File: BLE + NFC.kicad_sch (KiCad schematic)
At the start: 16 parts, among them IC5 nRF52832-CIAA-G-R7, Y2 Crystal_GND24

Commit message: progressed layout
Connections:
- net NRF_RXD: now also IC5.H3 (P0.16_/TRACEDATA[1]); no longer IC5.F4 (P0.11)
- net NRF_SDA: now also IC5.E7 (P0.05/_AIN3); no longer IC5.F6 (P0.07)
- net NRF_TXD: now also IC5.H4 (P0.15/TRACEDATA[2]); no longer IC5.H6 (P0.12)
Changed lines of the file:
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@@
     (stroke (width 0) (type default))
   )
-  (wire (pts (xy 176.53 107.95) (xy 179.07 107.95))
+  (wire (pts (xy 176.53 100.33) (xy 179.07 100.33))
     (stroke (width 0) (type default))
   )
@@
     (stroke (width 0) (type default))
   )
-  (wire (pts (xy 176.53 115.57) (xy 179.07 115.57))
+  (wire (pts (xy 176.53 120.65) (xy 179.07 120.65))
     (stroke (width 0) (type default))
   )
@@
     (stroke (width 0) (type default))
   )
-  (wire (pts (xy 176.53 110.49) (xy 179.07 110.49))
+  (wire (pts (xy 176.53 97.79) (xy 179.07 97.79))
     (stroke (width 0) (type default))
   )
@@
     )
   )
-  (hierarchical_label "NRF_TXD" (shape input) (at 179.07 107.95 0) (fields_autoplaced)
-    (effects (font (size 1.27 1.27)) (justify left))
-    (property "Intersheetrefs" "${INTERSHEET_REFS}" (at 189.3965 107.95 0)
-      (effects (font (size 1.27 1.27)) (justify left) hide)
-    )
-  )
-  (hierarchical_label "NRF_RXD" (shape input) (at 179.07 110.49 0) (fields_autoplaced)
-    (effects (font (size 1.27 1.27)) (justify left))
-    (property "Intersheetrefs" "${INTERSHEET_REFS}" (at 189.6989 110.49 0)
-      (effects (font (size 1.27 1.27)) (justify left) hide)
-    )
-  )
-  (hierarchical_label "NRF_SDA" (shape input) (at 179.07 115.57 0) (fields_autoplaced)
-    (effects (font (size 1.27 1.27)) (justify left))
-    (property "Intersheetrefs" "${INTERSHEET_REFS}" (at 190.2006 115.57 0)
+  (hierarchical_label "NRF_TXD" (shape input) (at 179.07 100.33 0) (fields_autoplaced)
+    (effects (font (size 1.27 1.27)) (justify left))
+    (property "Intersheetrefs" "${INTERSHEET_REFS}" (at 189.3965 97.79 0)
+      (effects (font (size 1.27 1.27)) (justify left) hide)
+    )
+  )
+  (hierarchical_label "NRF_RXD" (shape input) (at 179.07 97.79 0) (fields_autoplaced)
+    (effects (font (size 1.27 1.27)) (justify left))
+    (property "Intersheetrefs" "${INTERSHEET_REFS}" (at 189.6989 100.33 0)
+      (effects (font (size 1.27 1.27)) (justify left) hide)
+    )
+  )
+  (hierarchical_label "NRF_SDA" (shape input) (at 179.07 120.65 0) (fields_autoplaced)
+    (effects (font (size 1.27 1.27)) (justify left))
+    (property "Intersheetrefs" "${INTERSHEET_REFS}" (at 190.2006 120.65 0)
       (effects (font (size 1.27 1.27)) (justify left) hide)
     )
@@
   )
   (symbol (lib_id "ARMband:nRF52832-CIAA-G-R7") (at 120.65 71.12 0) (unit 1)
-    (in_bom yes) (on_board yes) (dnp no) (fields_autoplaced)
+    (in_bom yes) (on_board yes) (dnp no)
     (property "Reference" "IC5" (at 155.6259 140.97 0)
       (effects (font (size 1.27 1.27)) (justify left))

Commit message: added missing MFN numbers
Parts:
- AE1, C25, C8, IC5, L5, L6, Y2: sourced (none) -> y
- C25: MFN (none) -> 581-04025A101KAT2A62; sourced (none) -> y
- C8: MFN 187-CL05A475KQ5NRNC -> 187-CL05A475KQ5NRNC; sourced (none) -> y
- JP1: sourced (none) -> dc
- L4: MFN 810-MLZ1608E100MT -> 810-MLZ1608E100MT; sourced (none) -> y
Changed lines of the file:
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@@
+      (effects (font (size 1.27 1.27)) hide)
+    )
+    (property "sourced" "y" (at 120.65 71.12 0)
       (effects (font (size 1.27 1.27)) hide)
     )
@@
       (effects (font (size 1.27 1.27)) hide)
     )
-    (property "MFN" " 810-MLZ1608E100MT " (at 115.57 111.76 90)
+    (property "MFN" "810-MLZ1608E100MT " (at 115.57 111.76 90)
+      (effects (font (size 1.27 1.27)) hide)
+    )
+    (property "sourced" "y" (at 115.57 111.76 0)
       (effects (font (size 1.27 1.27)) hide)
     )
@@
       (effects (font (size 1.27 1.27)) hide)
     )
+    (property "sourced" "y" (at 52.07 50.8 0)
+      (effects (font (size 1.27 1.27)) hide)
+    )
     (pin "1")
     (pin "2")
@@
     )
     (property "MFN" "581-CX2016SA24DHLLG3 " (at 83.82 86.36 0)
+      (effects (font (size 1.27 1.27)) hide)
+    )
+    (property "sourced" "y" (at 83.82 86.36 0)
       (effects (font (size 1.27 1.27)) hide)
     )
@@
     )
     (property "MFN" "80-C0402C104M4V " (at 140.97 43.18 0)
+      (effects (font (size 1.27 1.27)) hide)
+    )
+    (property "sourced" "y" (at 140.97 43.18 0)
       (effects (font (size 1.27 1.27)) hide)
     )
@@
       (effects (font (size 1.27 1.27)) hide)
     )
+    (property "sourced" "y" (at 107.95 111.76 0)
+      (effects (font (size 1.27 1.27)) hide)
+    )
     (pin "1")
     (pin "2")
@@
     )
     (property "MFN" "603-AC0201JNPO9BN120 " (at 92.71 91.44 0)
+      (effects (font (size 1.27 1.27)) hide)
+    )
+    (property "sourced" "y" (at 92.71 91.44 0)
       (effects (font (size 1.27 1.27)) hide)
     )
@@
       (effects (font (size 1.27 1.27)) hide)
     )
-    (property "MFN" "" (at 38.1 25.4 0)
+    (property "MFN" "581-04025A101KAT2A62 " (at 38.1 25.4 0)
+      (effects (font (size 1.27 1.27)) hide)
+    )
+    (property "sourced" "y" (at 38.1 25.4 0)
       (effects (font (size 1.27 1.27)) hide)
     )
@@
       (effects (font (size 1.27 1.27)) hide)
     )
-    (property "MFN" " 187-CL05A475KQ5NRNC " (at 128.27 43.18 0)
+    (property "MFN" "187-CL05A475KQ5NRNC " (at 128.27 43.18 0)
+      (effects (font (size 1.27 1.27)) hide)
+    )
+    (property "sourced" "y" (at 128.27 43.18 0)
       (effects (font (size 1.27 1.27)) hide)
     )
@@
       (effects (font (size 1.27 1.27)) hide)
     )
+    (property "sourced" "y" (at 39.37 55.88 0)
+      (effects (font (size 1.27 1.27)) hide)
+    )
     (pin "1")
     (pin "2")
@@
       (effects (font (size 1.27 1.27)) hide)
     )
+    (property "sourced" "dc" (at 133.35 36.83 0)
+      (effects (font (size 1.27 1.27)) hide)
+    )
     (pin "1")
     (pin "2")
@@
       (effects (font (size 1.27 1.27)) hide)
     )
+    (property "sourced" "y" (at 74.93 91.44 0)
+      (effects (font (size 1.27 1.27)) hide)
+    )
     (pin "1")
     (pin "2")
@@
     )
     (property "MFN" "791-0402N0R8B160CT " (at 33.02 60.96 0)
+      (effects (font (size 1.27 1.27)) hide)
+    )
+    (property "sourced" "y" (at 33.02 60.96 0)
       (effects (font (size 1.27 1.27)) hide)
     )
@@
       (effects (font (size 1.27 1.27)) hide)
     )
+    (property "sourced" "y" (at 162.56 43.18 0)
+      (effects (font (size 1.27 1.27)) hide)
+    )
     (pin "1")
     (pin "2")
@@
       (effects (font (size 1.27 1.27)) hide)
     )
+    (property "sourced" "y" (at 90.17 115.57 0)
+      (effects (font (size 1.27 1.27)) hide)
+    )
     (pin "1")
     (pin "2")
@@
       (effects (font (size 1.27 1.27)) hide)
     )
-    (property "MFN" "" (at 38.1 30.48 0)
-      (effects (font (size 1.27 1.27)) hide)
-    )
+    (property "MFN" "581-04025A101KAT2A62 " (at 38.1 30.48 0)
+      (effects (font (size 1.27 1.27)) hide)
+    )
+    (property "sourced" "y" (at 38.1 30.48 0)
+      (effects (font (size 1.27 1.27)) hide)
+    )

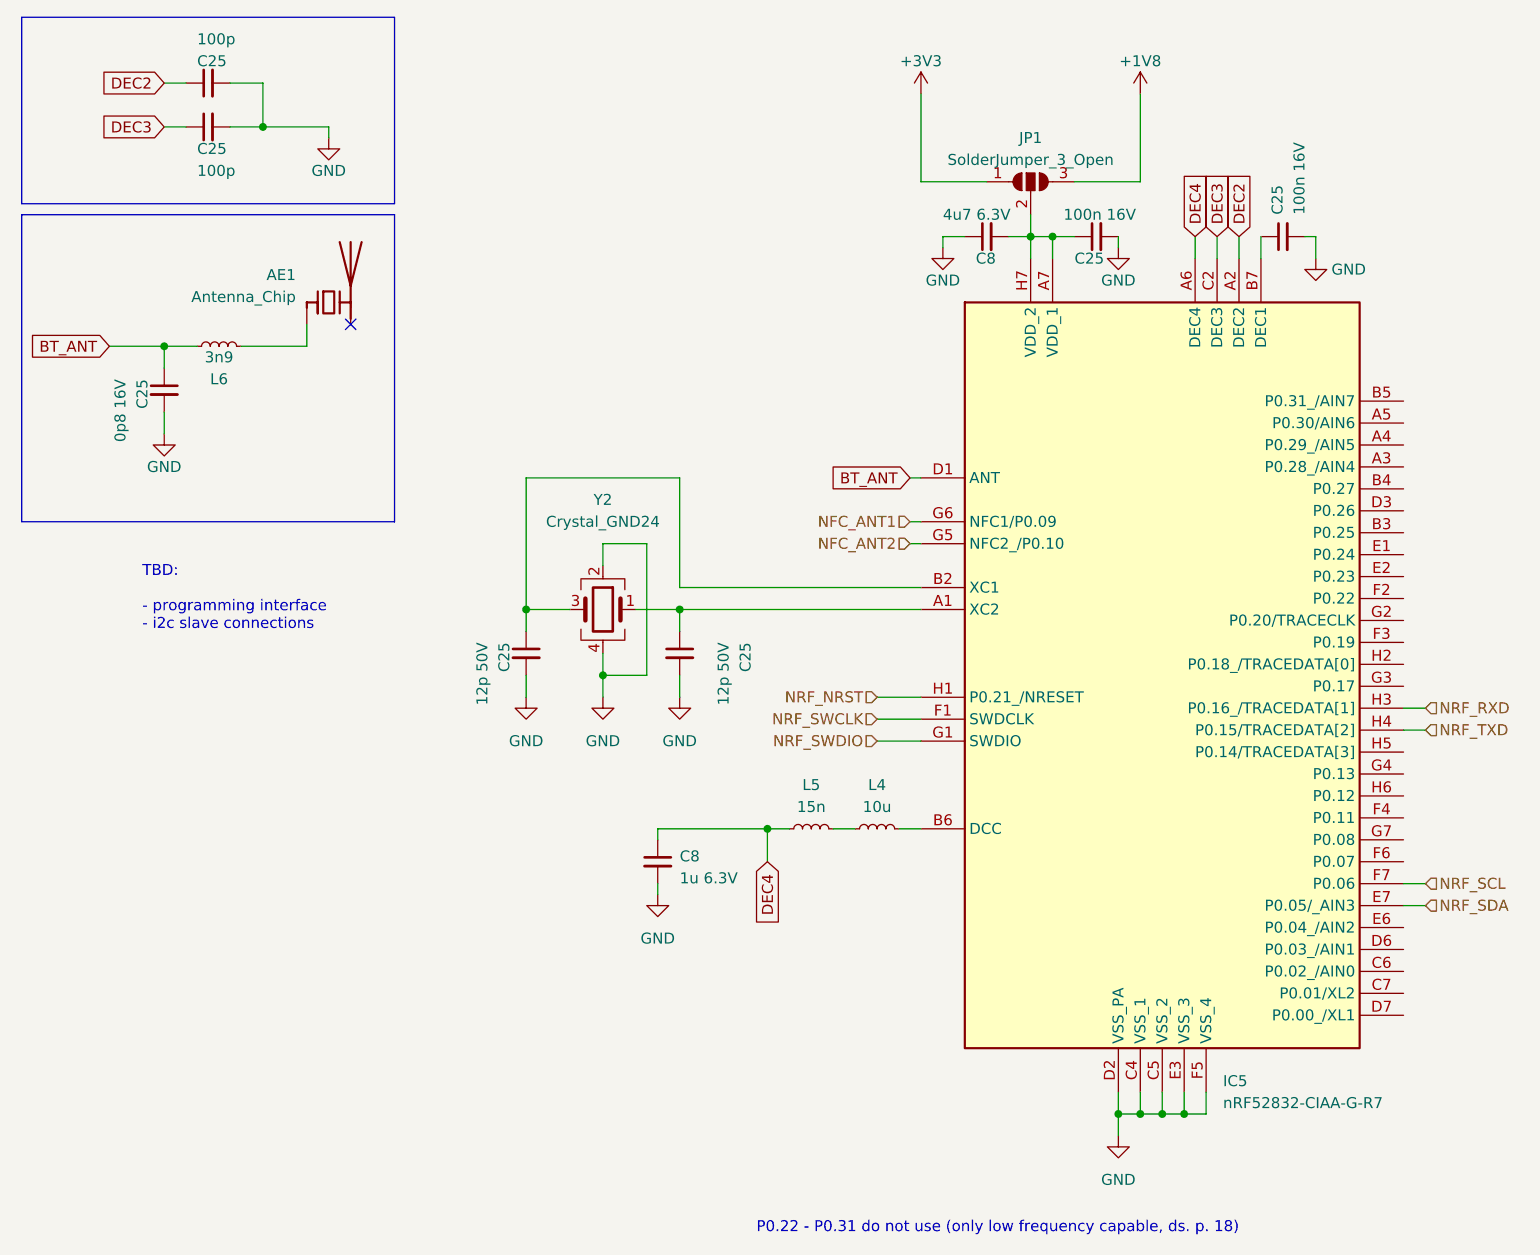
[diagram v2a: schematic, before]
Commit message: Update to KiCad 8 + Add/Fix voltage selector for nRF
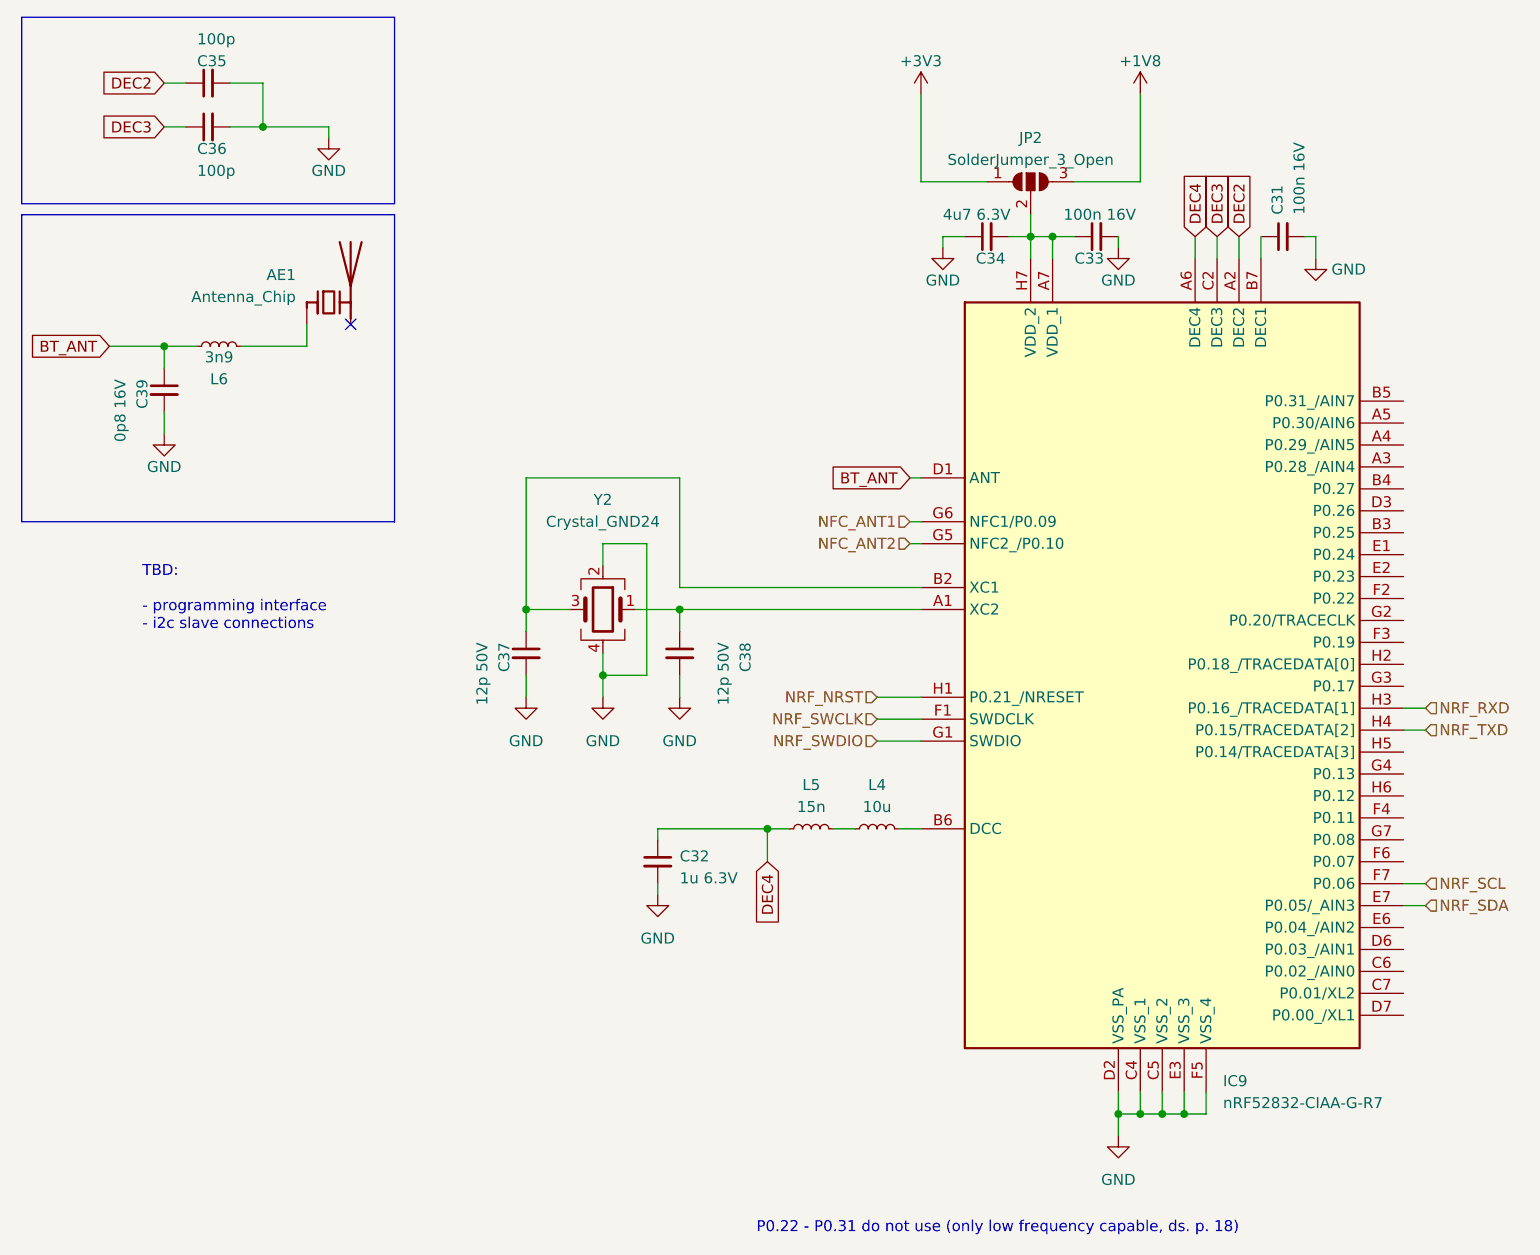
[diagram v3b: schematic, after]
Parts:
- JP2: renamed from JP1; footprint (none) -> Jumper:SolderJumper-3_P1.3mm_Open_RoundedPad1.0x1.5mm
- renumbered C25 to C31, C8 to C32, C25 to C33, C8 to C34, C25 to C35, C25 to C36, C25 to C37, C25 to C38, C25 to C39, IC5 to IC9
